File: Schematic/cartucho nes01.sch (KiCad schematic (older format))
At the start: 10 parts, among them U1 Teensy++2.0

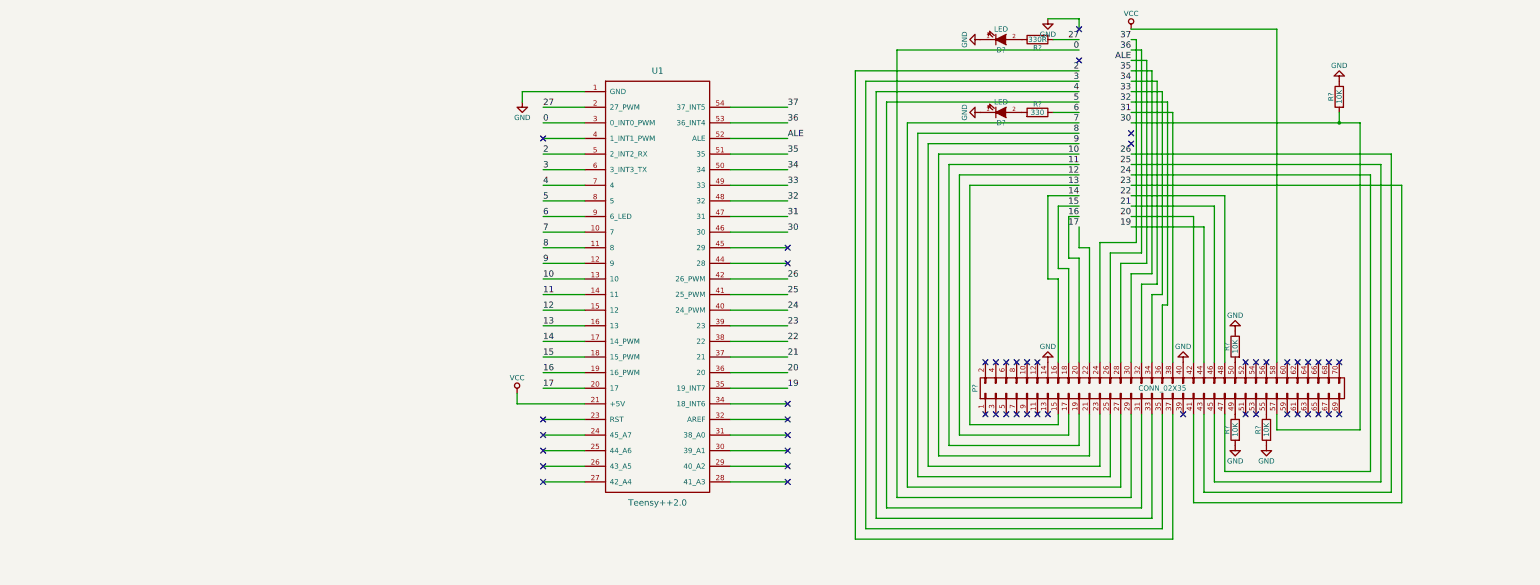
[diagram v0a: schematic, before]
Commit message: added schematic teensy++2
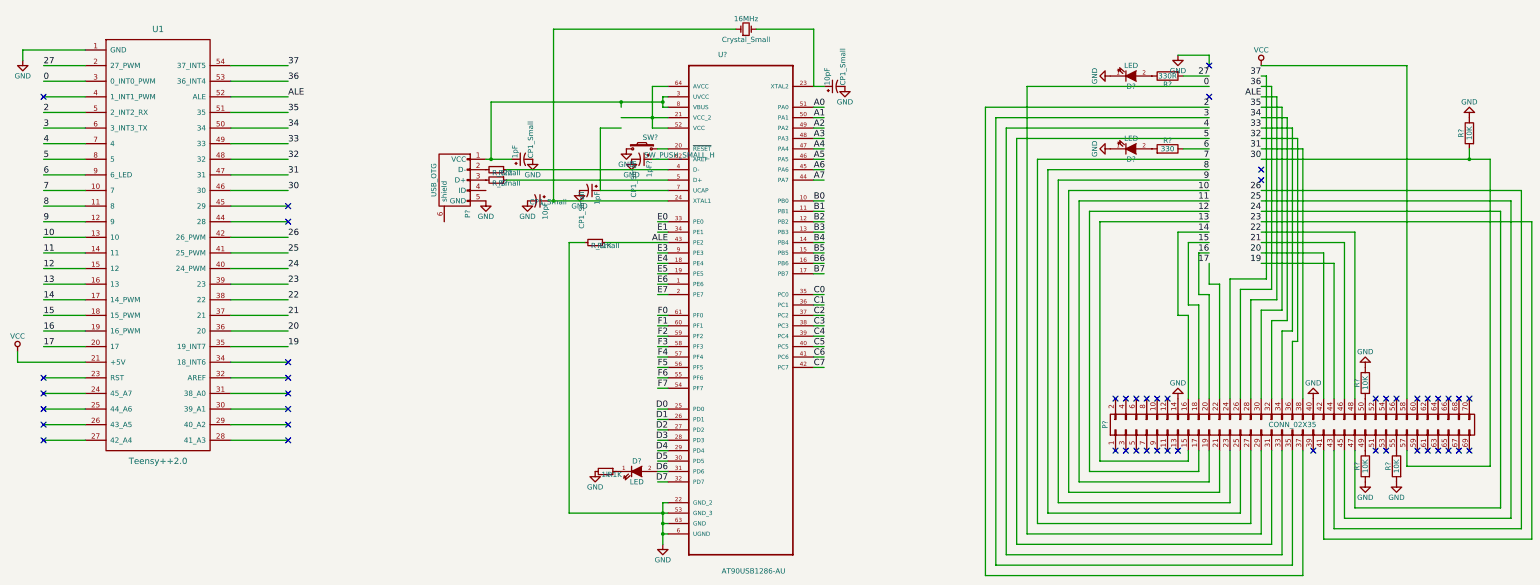
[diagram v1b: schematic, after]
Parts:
- added 10pF (x2), 1pF (x2), 1pF?: CP1_Small, symbol CP1_Small
- added 16MHz: Crystal_Small, symbol Crystal_Small
- added D?: LED, symbol LED
- added P?: USB_OTG, symbol USB_OTG
- added R1K: 1k, symbol R_Small
- added R1K, R22, R?: R_Small, symbol R_Small
- added SW?: SW_PUSH_SMALL_H, symbol SW_PUSH_SMALL_H
- added U?: AT90USB1286-AU, QFP80P1600X1600X120-64N, symbol AT90USB1286-AU
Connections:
- net labels added: A0, A1, A2, A3, A4, A5, A6, A7, B0, B1, B2, B3, B4, B5, B6, B7, C0, C1, C2, C3, C4, C5, C6, C7, D0, D1, D2, D3, D4, D5, D6, D7, E0, E1, E3, E4, E5, E6, E7, F0, F1, F2, F3, F4, F5, F6, F7
- wire segments 181 -> 260
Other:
- moved on the sheet: D?, P?, R?, U1
